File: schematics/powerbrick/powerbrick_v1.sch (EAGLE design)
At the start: 0 parts

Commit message: Libs and drawing update
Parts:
- added C1, C2: 1u, SparkFun-Capacitors:CAP_POL1206-KIT
- added C10: 4.7n, SparkFun-Capacitors:CAP1206
- added C3, C4, C5, C6, C7, C9: 100n, SparkFun-Capacitors:CAP1206
- added C8: 10u, SparkFun-Capacitors:CAP_POL1206-KIT
- added L1: 10uH, SparkFun-Passives:INDUCTORBOURNS_SRN6045
- added R1: 1M, SparkFun-Resistors:RESISTOR1206
- added SSR1, SSR2, SSR3: AQG22105, Skippy-Discrete:AQG22105
- added U$1: USB+SHIELD, SparkFun-Connectors:USB+SHIELD
- added U$2: SKIPPYTXT-PLC-10MM, skippy-logo:SKIPPYTXT-PLC-10MM
- added U1: ATXMEGA128C3-AU, atmel-xmega:ATXMEGA128C3-AU
- added U2: TC1262-3.3VDB, Skippy-IC:TC1262-3.3VDB
- added U3: PRTR5V0U2X, NXPSemiconductors:PRTR5V0U2X
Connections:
- new net 3.3V: C3.1, C4.1, C5.1, C6.1, C7.1, C8.+, C9.1, L1.2, U1.AVCC, U1.VCC
- new net GND: C1.-, C10.2, C2.-, C3.2, C4.2, C5.2, C6.2, C7.2, C8.-, C9.2, R1.1, U$1.GND, U1.GND, U2.GND_(TAB), U2.GND_(TAB)_2
- new net N$2: C2.+, L1.1, U2.VOUT
- new net N$5: C10.1, R1.2, U$1.S1, U$1.S2
- new net USB_DM: U$1.D-, U3U$1.IO2
- new net USB_DP: U$1.D+, U3U$1.IO1
- new net VCC: C1.+, U$1.VBUS, U2.VIN
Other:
- note added: "3.3V LDO regulator"
- note added: "USB ESD protection"
- note added: "USB input & shield decoupling"

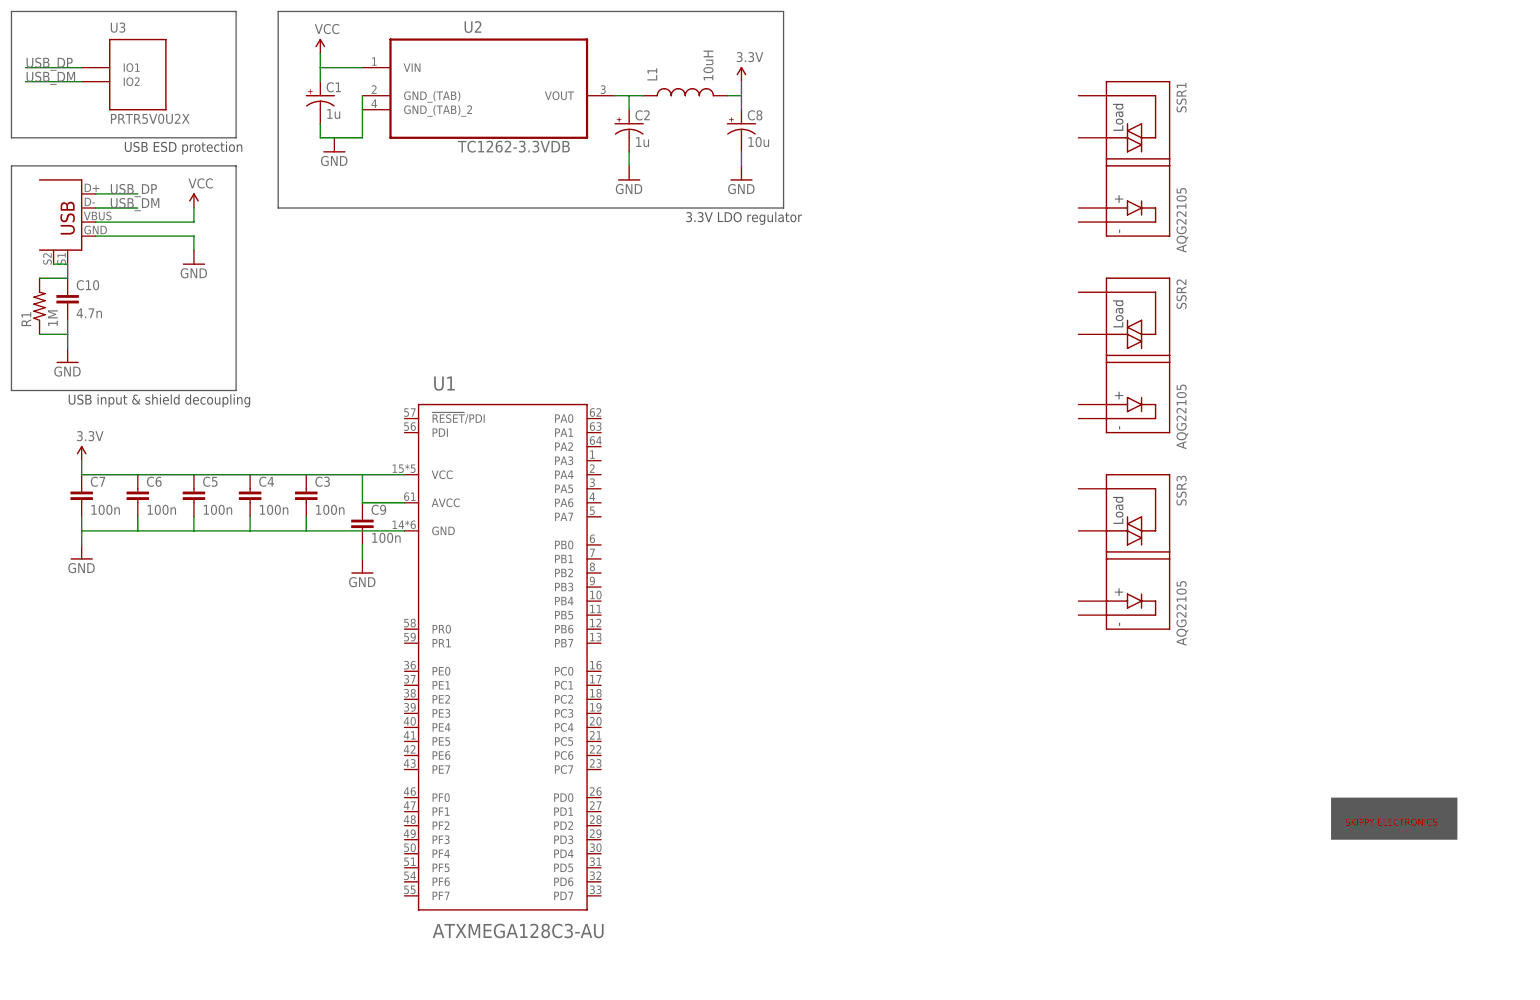
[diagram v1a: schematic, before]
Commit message: Powerbrick schematic update
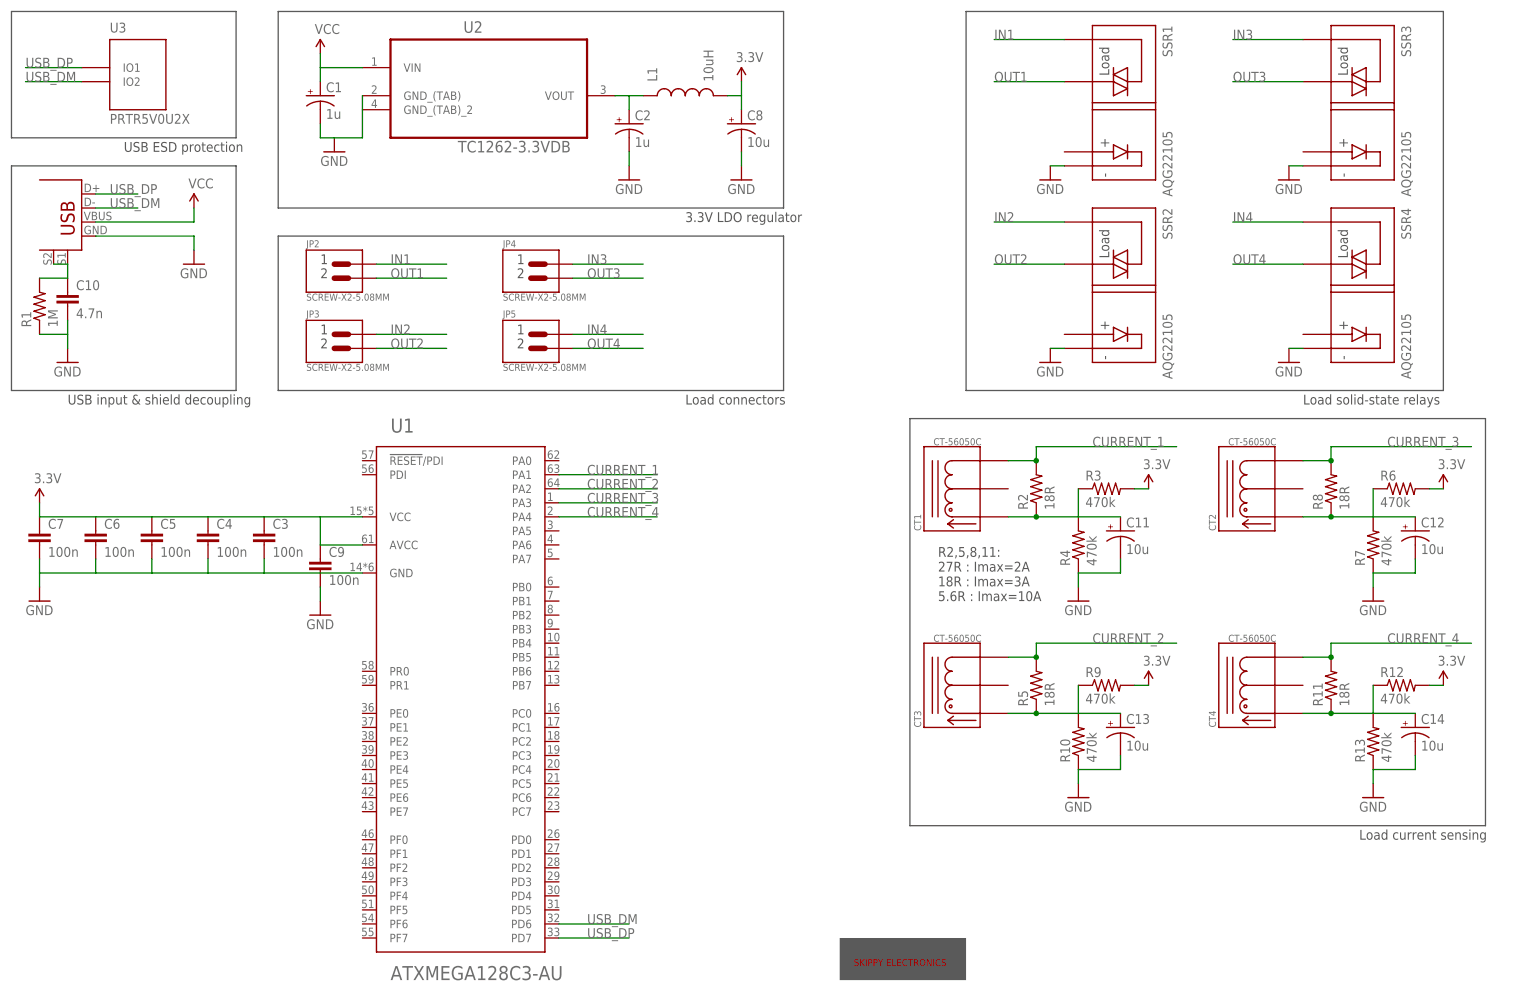
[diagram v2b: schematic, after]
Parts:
- added C11, C12, C13, C14: 10u, SparkFun-Capacitors:CAP_POL1206-KIT
- added CT1, CT2, CT3, CT4: CT-56050C, Skippy-Discrete:CT-56050C
- added JP2, JP3, JP4, JP5: SCREW-X2-5.08MM, Skippy-Connectors:SCREW-X2-5.08MM
- added R10, R12, R13, R3, R4, R6, R7, R9: 470k, SparkFun-Passives:RESISTOR1206
- added R11, R2, R5, R8: 18R, SparkFun-Passives:RESISTOR2512
- added SSR4: AQG22105, Skippy-Discrete:AQG22105
- SSR1, SSR2, SSR3: OC_FARNELL (none) -> 2095710
- renumbered U$1 to JP1
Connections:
- new net CURRENT_1: CT1.P$3, R2.2, U1.PA1
- new net CURRENT_2: CT3.P$3, R5.2, U1.PA2
- new net CURRENT_3: CT2.P$3, R8.2, U1.PA3
- new net CURRENT_4: CT4.P$3, R11.2, U1.PA4
- new net IN1: JP2.P$1, SSR1.P$1
- new net IN2: JP3.P$1, SSR2.P$1
- new net IN3: JP4.P$1, SSR3.P$1
- new net IN4: JP5.P$1, SSR4.P$1
- new net N$1: C12.+, CT2.P$1, R6.1, R7.2, R8.1
- new net N$3: C13.+, CT3.P$1, R10.2, R5.1, R9.1
- new net N$4: C11.+, CT1.P$1, R2.1, R3.1, R4.2
- new net N$6: C14.+, CT4.P$1, R11.1, R12.1, R13.2
- new net OUT1: JP2.P$2, SSR1.P$2
- new net OUT2: JP3.P$2, SSR2.P$2
- new net OUT3: JP4.P$2, SSR3.P$2
- new net OUT4: JP5.P$2, SSR4.P$2
- net 3.3V: now also R12.2, R3.2, R6.2, R9.2
- net GND: now also C11.-, C12.-, C13.-, C14.-, R10.1, R13.1, R4.1, R7.1, SSR1.P$4, SSR2.P$4, SSR3.P$4, SSR4.P$4
- net USB_DM: now also U1.PD6
- net USB_DP: now also U1.PD7
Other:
- note added: "Load connectors"
- note added: "Load current sensing"
- note added: "Load solid-state relays"
- note added: "R2,5,8,11: 27R : Imax=2A 18R : Imax=3A 5.6R : Imax=10A"
- moved on the sheet: C3, C4, C5, C6, C7, C9, SSR1, SSR2, SSR3, U1

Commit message: Schematics update
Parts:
- removed C12, C13, C14: 10u, SparkFun-Capacitors:CAP_POL1206-KIT
- removed CT2, CT3, CT4: CT-56050C, Skippy-Discrete:CT-56050C
- removed R10, R12, R13, R6, R7, R9: 470k, SparkFun-Passives:RESISTOR1206
- removed R11, R5, R8: 18R, SparkFun-Passives:RESISTOR2512
- added D1: Red, SparkFun-LED:LED5MM
- added JP6: (no value), SparkFun-Connectors:M04POLAR_LOCK
- added R14: 150R, SparkFun-Passives:RESISTOR0805-RES
- added R15, R16, R17, R18: 10k, SparkFun-Passives:RESISTOR0805-RES
- added U4: ULN2003LVPWR, Skippy-IC:ULN2003LVPWR
- added U5: MCP9800A0T-M/OT, Skippy-IC:MCP9800A0T-M/OT
- C10, C3, C4, C5, C6, C7, C9: device SparkFun-Capacitors:CAP1206 -> SparkFun-Capacitors:CAP0805
- R1: device SparkFun-Resistors:RESISTOR1206 -> SparkFun-Passives:RESISTOR0805-RES
- R3, R4: device SparkFun-Passives:RESISTOR1206 -> SparkFun-Passives:RESISTOR0805-RES
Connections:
- removed net CURRENT_2: CT3.P$3, R5.2, U1.PA2
- removed net CURRENT_3: CT2.P$3, R8.2, U1.PA3
- removed net CURRENT_4: CT4.P$3, R11.2, U1.PA4
- removed net N$1: C12.+, CT2.P$1, R6.1, R7.2, R8.1
- removed net N$3: C13.+, CT3.P$1, R10.2, R5.1, R9.1
- removed net N$6: C14.+, CT4.P$1, R11.1, R12.1, R13.2
- new net BJT1: U1.PB3, U4.IN1
- new net BJT2: U1.PB2, U4.IN2
- new net BJT3: U1.PB1, U4.IN3
- new net BJT4: U1.PB0, U4.IN4
- new net CTRL_1: SSR1.P$4, U4.OUT1
- new net CTRL_2: SSR2.P$4, U4.OUT2
- new net CTRL_3: SSR3.P$4, U4.OUT3
- new net CTRL_4: SSR4.P$4, U4.OUT4
- new net N$11: R14.2, U1.PD0
- new net N$12: D1.A, R14.1
- new net SCL0: JP6.3, R18.2, U1.PC1
- new net SCL1: R16.2, U1.PE1, U5.SCLK
- new net SDA0: JP6.2, R17.2, U1.PC0
- new net SDA1: R15.2, U1.PE0, U5.SDA
- new net TEMP_ALERT: U1.PE2, U5.ALERT
- net 3.3V: now also JP6.1, R15.1, R16.1, R17.1, R18.1, U5.VDD; no longer R12.2, R6.2, R9.2
- net GND: now also D1.C, JP6.4, U4.GND, U4.IN5, U4.IN6, U4.IN7, U5.GND; no longer C12.-, C13.-, C14.-, R10.1, R13.1, R7.1, SSR1.P$4, SSR2.P$4, SSR3.P$4, SSR4.P$4
- net VCC: now also SSR1.P$3, SSR2.P$3, SSR3.P$3, SSR4.P$3
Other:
- note added: "Ext. I2C bus"
- note added: "Place close to SSRs"
- note added: "SSR control"
- note added: "Temp. sensor"
- moved on the sheet: C11, CT1, JP2, JP3, JP4, JP5, R2, R3, R4

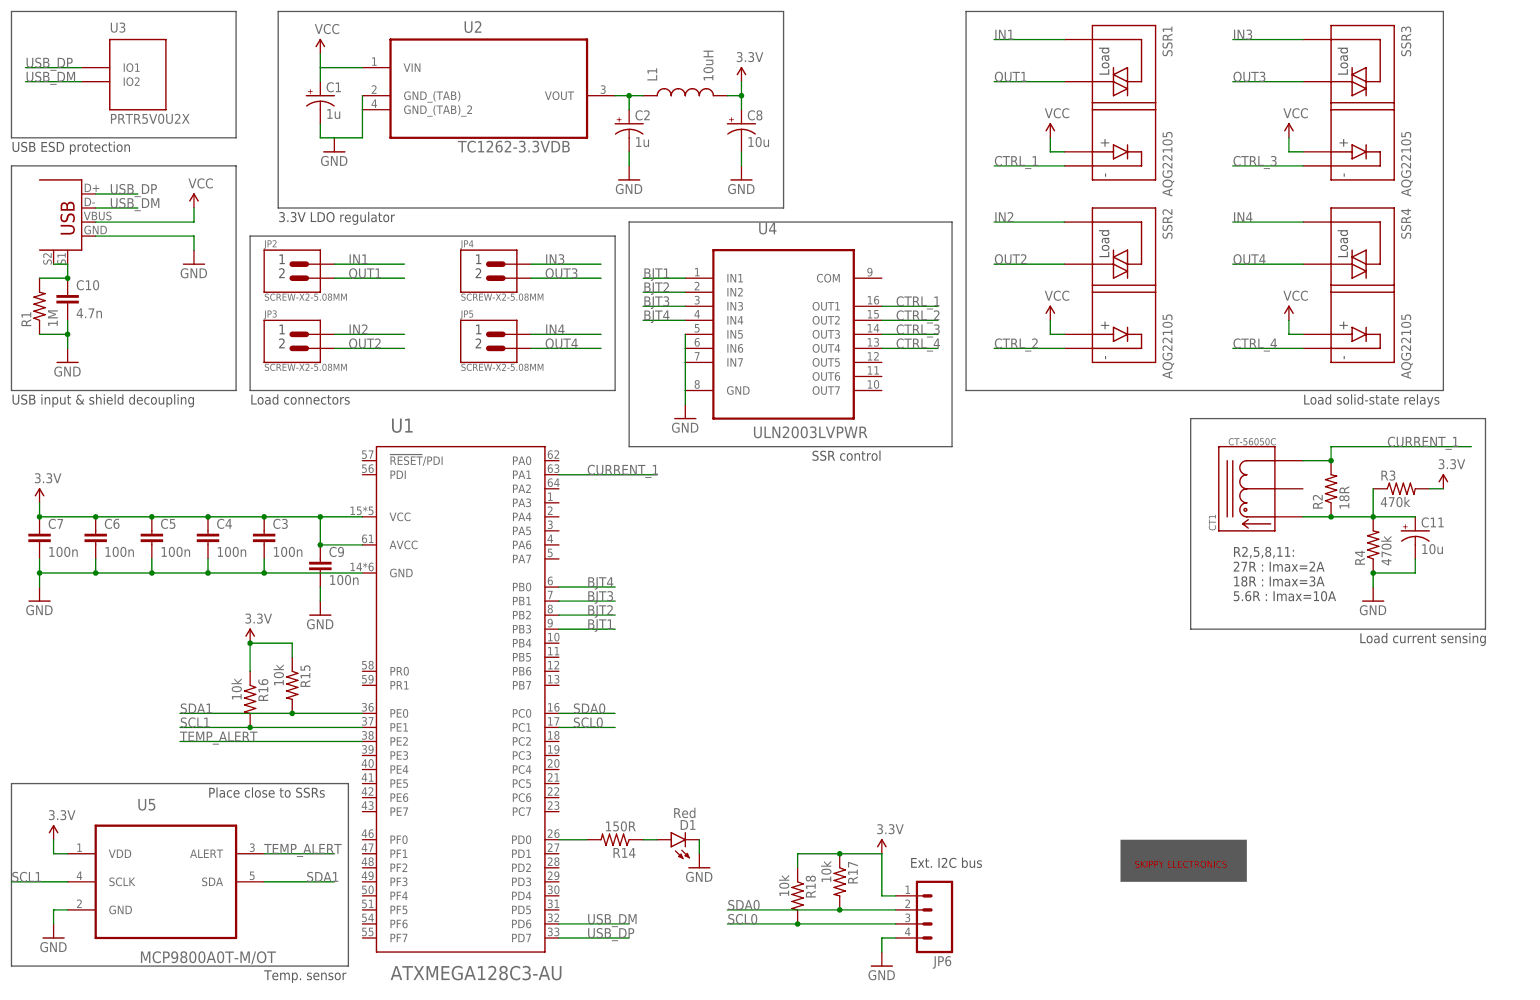
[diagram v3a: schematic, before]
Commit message: Added ISP header
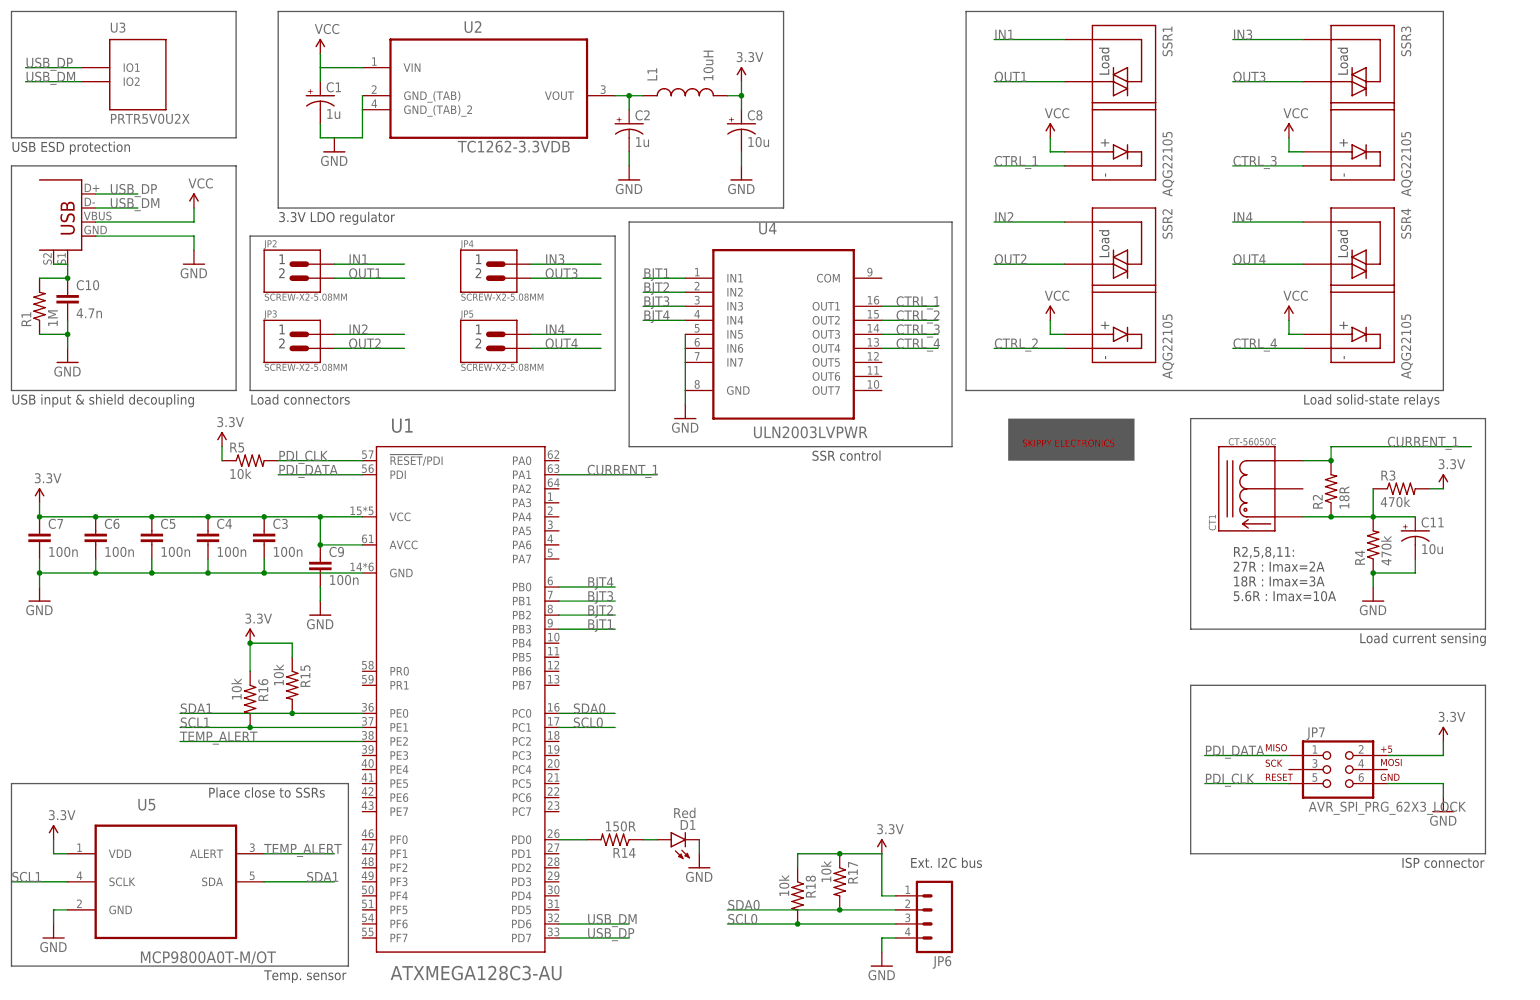
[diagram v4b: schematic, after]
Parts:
- added JP7: AVR_SPI_PRG_62X3_LOCK, SparkFun-Connectors:AVR_SPI_PRG_62X3_LOCK
- added R5: 10k, SparkFun-Passives:RESISTOR0805-RES
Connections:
- new net PDI_CLK: JP7.5, R5.2, U1.!RESET!/PDI
- new net PDI_DATA: JP7.1, U1.PDI
- net 3.3V: now also JP7.2, R5.1
- net GND: now also JP7.6
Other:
- note added: "ISP connector"
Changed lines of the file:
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@@
 <part name="R17" library="SparkFun-Passives" deviceset="RESISTOR" device="0805-RES" value="10k"/>
 <part name="R18" library="SparkFun-Passives" deviceset="RESISTOR" device="0805-RES" value="10k"/>
+<part name="JP7" library="SparkFun-Connectors" deviceset="AVR_SPI_PRG_6" device="2X3_LOCK"/>
+<part name="SUPPLY6" library="SparkFun-Aesthetics" deviceset="3.3V" device=""/>
+<part name="GND9" library="SparkFun-Aesthetics" deviceset="GND" device=""/>
+<part name="SUPPLY7" library="SparkFun-Aesthetics" deviceset="3.3V" device=""/>
+<part name="R5" library="SparkFun-Passives" deviceset="RESISTOR" device="0805-RES" value="10k"/>
 </parts>
 <sheets>
@@
 <wire x1="114.3" y1="99.06" x2="114.3" y2="139.7" width="0.1524" layer="97"/>
 <text x="147.32" y="96.52" size="1.778" layer="97">SSR control</text>
+<wire x1="215.9" y1="55.88" x2="269.24" y2="55.88" width="0.1524" layer="97"/>
+<wire x1="269.24" y1="55.88" x2="269.24" y2="25.4" width="0.1524" layer="97"/>
+<wire x1="269.24" y1="25.4" x2="215.9" y2="25.4" width="0.1524" layer="97"/>
+<wire x1="215.9" y1="25.4" x2="215.9" y2="55.88" width="0.1524" layer="97"/>
+<text x="254" y="22.86" size="1.778" layer="97">ISP connector</text>
 </plain>
 <instances>
@@
 </instance>
 <instance part="GND5" gate="1" x="134.62" y="147.32"/>
-<instance part="U$2" gate="G$1" x="215.9" y="22.86"/>
+<instance part="U$2" gate="G$1" x="195.58" y="99.06"/>
 <instance part="C10" gate="G$1" x="12.7" y="124.46"/>
 <instance part="R1" gate="G$1" x="7.62" y="124.46" rot="R90"/>
@@
 <instance part="R17" gate="G$1" x="152.4" y="20.32" rot="R270"/>
 <instance part="R18" gate="G$1" x="144.78" y="17.78" rot="R270"/>
+<instance part="JP7" gate="G$1" x="241.3" y="40.64"/>
+<instance part="SUPPLY6" gate="G$1" x="261.62" y="45.72"/>
+<instance part="GND9" gate="1" x="261.62" y="33.02"/>
+<instance part="SUPPLY7" gate="G$1" x="40.64" y="99.06"/>
+<instance part="R5" gate="G$1" x="45.72" y="96.52"/>
 </instances>
 <busses>
@@
 <wire x1="160.02" y1="10.16" x2="160.02" y2="7.62" width="0.1524" layer="91"/>
 <pinref part="GND14" gate="1" pin="GND"/>
+</segment>
+<segment>
+<pinref part="JP7" gate="G$1" pin="6"/>
+<wire x1="251.46" y1="38.1" x2="261.62" y2="38.1" width="0.1524" layer="91"/>
+<wire x1="261.62" y1="38.1" x2="261.62" y2="35.56" width="0.1524" layer="91"/>
+<pinref part="GND9" gate="1" pin="GND"/>
 </segment>
 </net>
@@
 <junction x="152.4" y="25.4"/>
 </segment>
+<segment>
+<pinref part="JP7" gate="G$1" pin="2"/>
+<wire x1="251.46" y1="43.18" x2="261.62" y2="43.18" width="0.1524" layer="91"/>
+<wire x1="261.62" y1="43.18" x2="261.62" y2="45.72" width="0.1524" layer="91"/>
+<pinref part="SUPPLY6" gate="G$1" pin="3.3V"/>
+</segment>
+<segment>
+<pinref part="SUPPLY7" gate="G$1" pin="3.3V"/>
+<wire x1="40.64" y1="96.52" x2="40.64" y2="99.06" width="0.1524" layer="91"/>
+<pinref part="R5" gate="G$1" pin="1"/>
+</segment>
 </net>
 <net name="VCC" class="0">
@@
 </segment>
 </net>
+<net name="PDI_DATA" class="0">
+<segment>
+<pinref part="U1" gate="G$1" pin="PDI"/>
+<wire x1="66.04" y1="93.98" x2="50.8" y2="93.98" width="0.1524" layer="91"/>
+<label x="50.8" y="93.98" size="1.778" layer="95"/>
+</segment>
+<segment>
+<pinref part="JP7" gate="G$1" pin="1"/>
+<wire x1="233.68" y1="43.18" x2="218.44" y2="43.18" width="0.1524" layer="91"/>
+<label x="218.44" y="43.18" size="1.778" layer="95"/>
+</segment>
+</net>
+<net name="PDI_CLK" class="0">
+<segment>
+<pinref part="U1" gate="G$1" pin="!RESET!/PDI"/>
+<wire x1="50.8" y1="96.52" x2="66.04" y2="96.52" width="0.1524" layer="91"/>
+<label x="50.8" y="96.52" size="1.778" layer="95"/>
+<pinref part="R5" gate="G$1" pin="2"/>
+</segment>
+<segment>
+<pinref part="JP7" gate="G$1" pin="5"/>
+<wire x1="233.68" y1="38.1" x2="218.44" y2="38.1" width="0.1524" layer="91"/>
+<label x="218.44" y="38.1" size="1.778" layer="95"/>
+</segment>
+</net>
